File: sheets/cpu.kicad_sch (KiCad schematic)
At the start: 6 parts, among them J1 BEER, U1 uPD43256AGU-12L, U2 uPD43256AGU-12L, U3 HD68HC000P, U4 NEO-C1

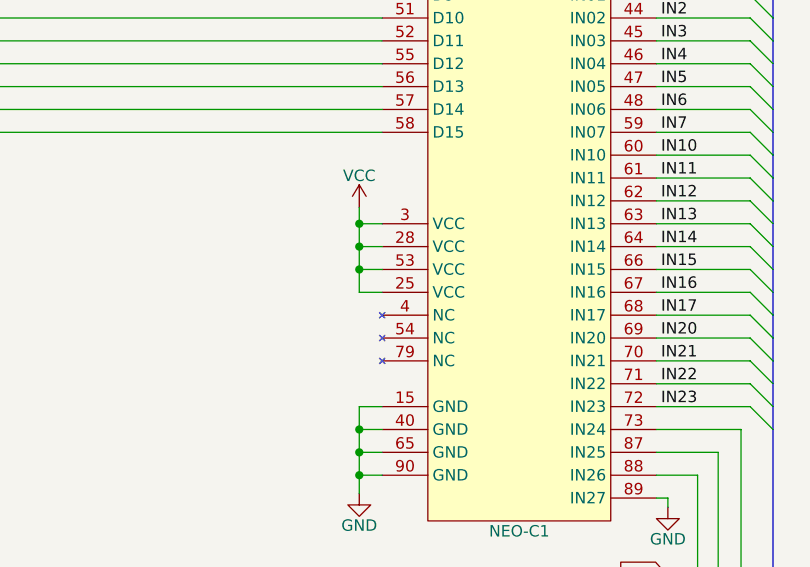
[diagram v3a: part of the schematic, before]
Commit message: fixed wrong pin number on Neo-C1
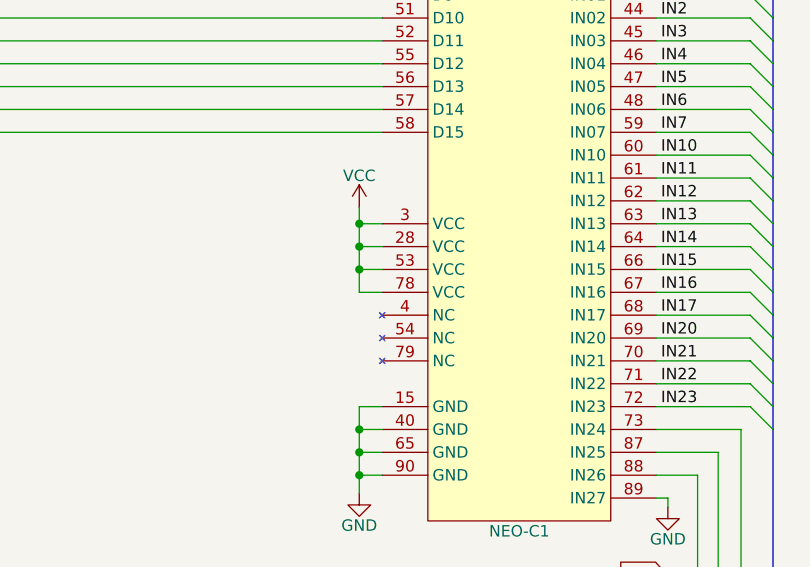
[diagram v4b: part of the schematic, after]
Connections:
- net VCC: now also U4.78 (VCC); no longer U4.25 (VCC)
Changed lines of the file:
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@@
     (pin "24")
-    (pin "25")
     (pin "25")
     (pin "26")
@@
     (pin "76")
     (pin "77")
+    (pin "78")
     (pin "79")
     (pin "8")

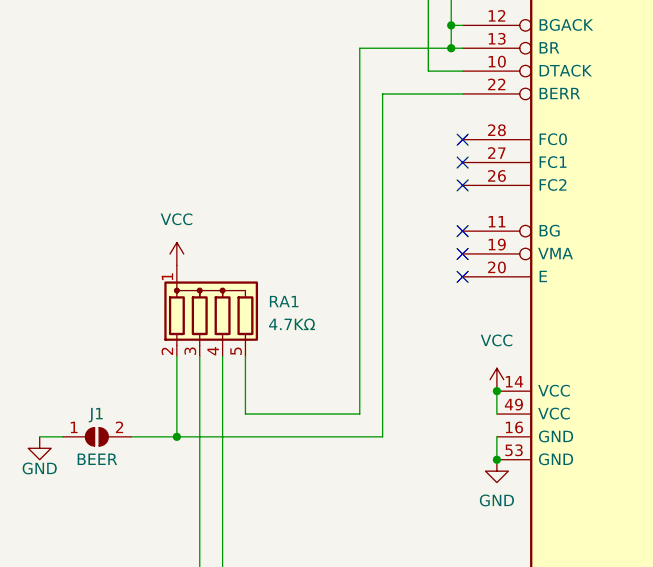
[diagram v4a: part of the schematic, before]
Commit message: Added missing J3 and J4 for EVEN pin from LSPC2. Missing from original schematics Fixed RA1 being wrong way U38 pins 12/13 to VCC
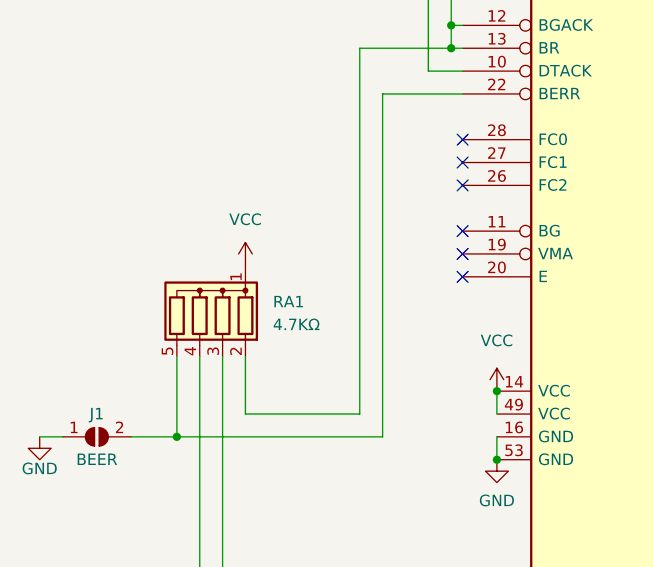
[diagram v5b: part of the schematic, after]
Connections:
- net HALT: now also RA1.4 (R3); no longer RA1.3 (R2)
- net RESET: now also RA1.3 (R2); no longer RA1.4 (R3)
- net at J1.2 (B), U3.22 (BERR): now also RA1.5 (R4); no longer RA1.2 (R1)
- net at U3.12 (BGACK), U3.13 (BR), U3.23 (IPL2): now also RA1.2 (R1); no longer RA1.5 (R4)
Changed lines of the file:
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@@
     (effects (font (size 1.27 1.27)) (justify left))
   )
-  (symbol (lib_id "Device:R_Network04") (at 62.992 140.208 0) (unit 1)
-    (in_bom yes) (on_board yes) (fields_autoplaced)
-    (property "Reference" "RA1" (id 0) (at 68.072 139.1919 0)
-      (effects (font (size 1.27 1.27)) (justify left))
-    )
-    (property "Value" "4.7KΩ" (id 1) (at 68.072 141.7319 0)
-      (effects (font (size 1.27 1.27)) (justify left))
-    )
-    (property "Footprint" "Resistor_THT:R_Array_SIP5" (id 2) (at 69.977 140.208 90)
-      (effects (font (size 1.27 1.27)) hide)
-    )
-    (property "Datasheet" "" (id 3) (at 62.992 140.208 0)
+  (symbol (lib_id "Device:R_Network04") (at 60.452 140.208 0) (mirror y) (unit 1)
+    (in_bom yes) (on_board yes) (fields_autoplaced)
+    (property "Reference" "RA1" (id 0) (at 68.58 139.1919 0)
+      (effects (font (size 1.27 1.27)) (justify right))
+    )
+    (property "Value" "4.7KΩ" (id 1) (at 68.58 141.7319 0)
+      (effects (font (size 1.27 1.27)) (justify right))
+    )
+    (property "Footprint" "Resistor_THT:R_Array_SIP5" (id 2) (at 53.467 140.208 90)
+      (effects (font (size 1.27 1.27)) hide)
+    )
+    (property "Datasheet" "" (id 3) (at 60.452 140.208 0)
       (effects (font (size 1.27 1.27)) hide)
     )
@@
     (pin "1")
   )
-  (symbol (lib_id "power:VCC") (at 57.912 135.128 0) (unit 1)
-    (in_bom yes) (on_board yes) (fields_autoplaced)
-    (property "Reference" "#PWR0104" (id 0) (at 57.912 138.938 0)
-      (effects (font (size 1.27 1.27)) hide)
-    )
-    (property "Value" "VCC" (id 1) (at 57.912 130.048 0))
-    (property "Footprint" "" (id 2) (at 57.912 135.128 0)
-      (effects (font (size 1.27 1.27)) hide)
-    )
-    (property "Datasheet" "" (id 3) (at 57.912 135.128 0)
-      (effects (font (size 1.27 1.27)) hide)
-    )
+  (symbol (lib_id "power:VCC") (at 65.532 135.128 0) (unit 1)
+    (in_bom yes) (on_board yes) (fields_autoplaced)
+    (property "Reference" "#PWR0104" (id 0) (at 65.532 138.938 0)
+      (effects (font (size 1.27 1.27)) hide)
+    )
+    (property "Value" "VCC" (id 1) (at 65.532 130.048 0))
+    (property "Footprint" "" (id 2) (at 65.532 135.128 0)
+      (effects (font (size 1.27 1.27)) hide)
+    )
+    (property "Datasheet" "" (id 3) (at 65.532 135.128 0)
+      (effects (font (size 1.27 1.27)) hide)
+    )

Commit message: Sync footprints from Nightly Build
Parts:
- U1, U2: footprint Package_DIP:DIP-28_W15.24mm -> 1_NeoGeoLibrary:43256
- U3: footprint Package_DIP:DIP-64_W25.4mm -> 1_NeoGeoLibrary:68000
- U4: footprint Package_LCC:PLCC-84 -> 1_NeoGeoLibrary:NEO-C1
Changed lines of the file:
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@@
     (property "Reference" "U4" (id 0) (at 295.275 54.991 0))
     (property "Value" "NEO-C1" (id 1) (at 304.038 196.723 0))
-    (property "Footprint" "Package_LCC:PLCC-84" (id 2) (at 304.038 114.3 0)
+    (property "Footprint" "1_NeoGeoLibrary:NEO-C1" (id 2) (at 304.038 114.3 0)
       (effects (font (size 1.27 1.27)) hide)
     )
@@
       (effects (font (size 1.27 1.27)) (justify left))
     )
-    (property "Footprint" "Package_DIP:DIP-28_W15.24mm" (id 2) (at 197.612 118.618 0)
+    (property "Footprint" "1_NeoGeoLibrary:43256" (id 2) (at 197.612 118.618 0)
       (effects (font (size 1.27 1.27)) hide)
     )
@@
       (effects (font (size 1.27 1.27)) (justify left))
     )
-    (property "Footprint" "Package_DIP:DIP-28_W15.24mm" (id 2) (at 197.612 169.672 0)
+    (property "Footprint" "1_NeoGeoLibrary:43256" (id 2) (at 197.612 169.672 0)
       (effects (font (size 1.27 1.27)) hide)
     )
@@
     (property "Reference" "U3" (id 0) (at 98.552 88.138 0))
     (property "Value" "HD68HC000P" (id 1) (at 126.492 88.138 0))
-    (property "Footprint" "Package_DIP:DIP-64_W25.4mm" (id 2) (at 115.062 146.558 0)
-      (effects (font (size 1.27 1.27)) hide)
-    )
+    (property "Footprint" "1_NeoGeoLibrary:68000" (id 2) (at 115.062 146.558 0)
+      (effects (font (size 1.27 1.27)) hide)
+    )

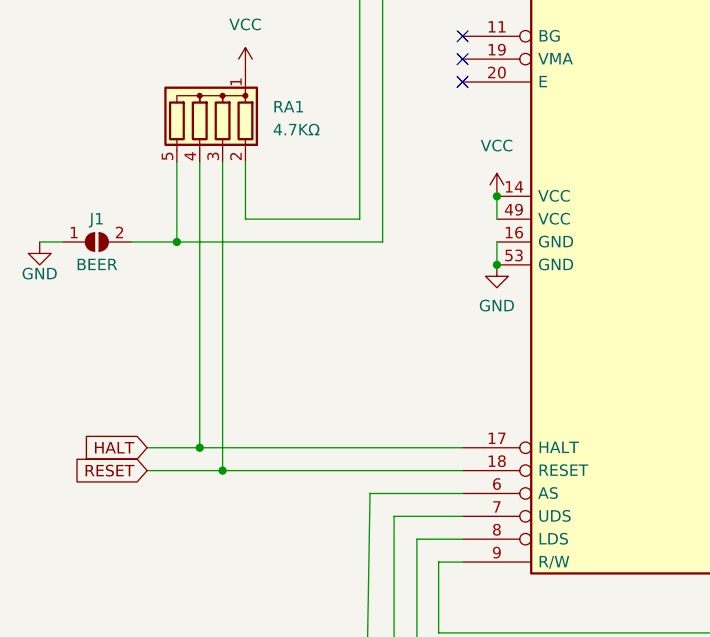
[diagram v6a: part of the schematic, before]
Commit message: 1. Swap Halt / Reset on RA1 2. Added more Power Caps 3. Change Audio socket Left/Right around 4. Added Ferrite Beads to Audio Signals 5. Added Ferrite Beads to Video Signals
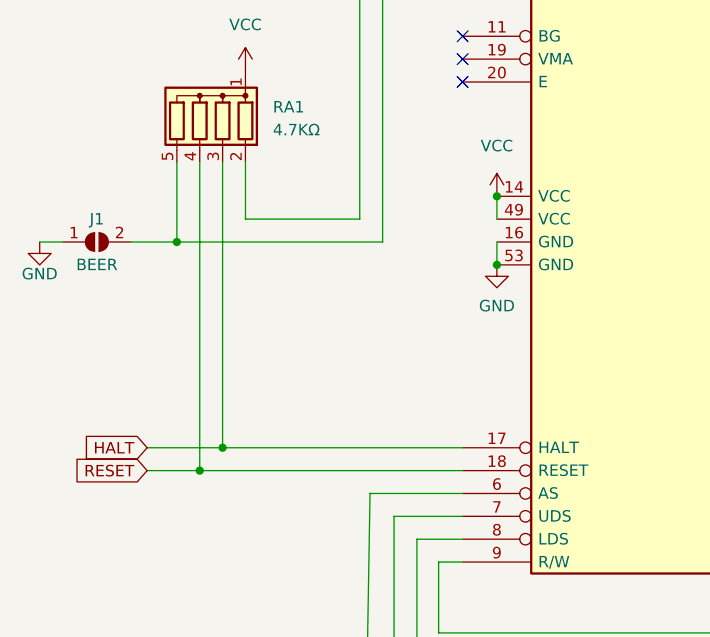
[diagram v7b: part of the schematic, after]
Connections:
- net HALT: now also RA1.3 (R2); no longer RA1.4 (R3)
- net RESET: now also RA1.4 (R3); no longer RA1.3 (R2)
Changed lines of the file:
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@@
   (junction (at 88.392 110.998) (diameter 0) (color 0 0 0 0)
   )
+  (junction (at 62.992 177.038) (diameter 0) (color 0 0 0 0)
+  )
   (junction (at 286.258 187.96) (diameter 0) (color 0 0 0 0)
   )
@@
   (junction (at 93.472 156.718) (diameter 0) (color 0 0 0 0)
   )
+  (junction (at 60.452 179.578) (diameter 0) (color 0 0 0 0)
+  )
   (junction (at 200.406 195.072) (diameter 0) (color 0 0 0 0)
   )
@@
   )
   (junction (at 286.258 185.42) (diameter 0) (color 0 0 0 0)
-  )
-  (junction (at 62.992 179.578) (diameter 0) (color 0 0 0 0)
-  )
-  (junction (at 60.452 177.038) (diameter 0) (color 0 0 0 0)
   )
   (junction (at 286.258 165.1) (diameter 0) (color 0 0 0 0)
@@
     (stroke (width 0) (type default) (color 0 0 0 0))
   )
-  (wire (pts (xy 54.61 177.038) (xy 60.452 177.038))
+  (wire (pts (xy 54.61 177.038) (xy 62.992 177.038))
     (stroke (width 0) (type default) (color 0 0 0 0))
   )
@@
     (stroke (width 0) (type default) (color 0 0 0 0))
   )
-  (wire (pts (xy 60.452 145.288) (xy 60.452 177.038))
+  (wire (pts (xy 62.992 145.288) (xy 62.992 177.038))
     (stroke (width 0) (type default) (color 0 0 0 0))
   )
@@
     (stroke (width 0) (type default) (color 0 0 0 0))
   )
+  (wire (pts (xy 60.452 179.578) (xy 89.662 179.578))
+    (stroke (width 0) (type default) (color 0 0 0 0))
+  )
   (wire (pts (xy 162.306 204.724) (xy 167.386 204.724))
     (stroke (width 0) (type default) (color 0 0 0 0))
@@
     (stroke (width 0) (type default) (color 0 0 0 0))
   )
-  (wire (pts (xy 54.61 179.578) (xy 62.992 179.578))
+  (wire (pts (xy 54.61 179.578) (xy 60.452 179.578))
     (stroke (width 0) (type default) (color 0 0 0 0))
   )
@@
     (stroke (width 0) (type default) (color 0 0 0 0))
   )
-  (wire (pts (xy 62.992 145.288) (xy 62.992 179.578))
+  (wire (pts (xy 60.452 145.288) (xy 60.452 179.578))
     (stroke (width 0) (type default) (color 0 0 0 0))
   )
@@
     (stroke (width 0) (type default) (color 0 0 0 0))
   )
+  (wire (pts (xy 62.992 177.038) (xy 89.662 177.038))
+    (stroke (width 0) (type default) (color 0 0 0 0))
+  )
   (wire (pts (xy 288.798 78.74) (xy 160.02 78.74))
     (stroke (width 0) (type default) (color 0 0 0 0))
@@
     (stroke (width 0) (type default) (color 0 0 0 0))
   )
-  (wire (pts (xy 60.452 177.038) (xy 89.662 177.038))
-    (stroke (width 0) (type default) (color 0 0 0 0))
-  )
   (wire (pts (xy 140.462 169.418) (xy 150.876 169.418))
     (stroke (width 0) (type default) (color 0 0 0 0))
@@
     (stroke (width 0) (type default) (color 0 0 0 0))
   )
-  (wire (pts (xy 62.992 179.578) (xy 89.662 179.578))
-    (stroke (width 0) (type default) (color 0 0 0 0))
-  )

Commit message: Sync Footprints from Nightly
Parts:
- J1: footprint Jumper:SolderJumper-2_P1.3mm_Open_Pad1.0x1.5mm -> 1_NeoGeoLibrary:J2
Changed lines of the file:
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@@
     (property "Reference" "J1" (id 0) (at 49.022 151.638 0))
     (property "Value" "BEER" (id 1) (at 49.022 156.718 0))
-    (property "Footprint" "Jumper:SolderJumper-2_P1.3mm_Open_Pad1.0x1.5mm" (id 2) (at 49.022 154.178 0)
+    (property "Footprint" "1_NeoGeoLibrary:J2" (id 2) (at 49.022 154.178 0)
       (effects (font (size 1.27 1.27)) hide)
     )
